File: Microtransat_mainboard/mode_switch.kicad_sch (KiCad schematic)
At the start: 3 parts

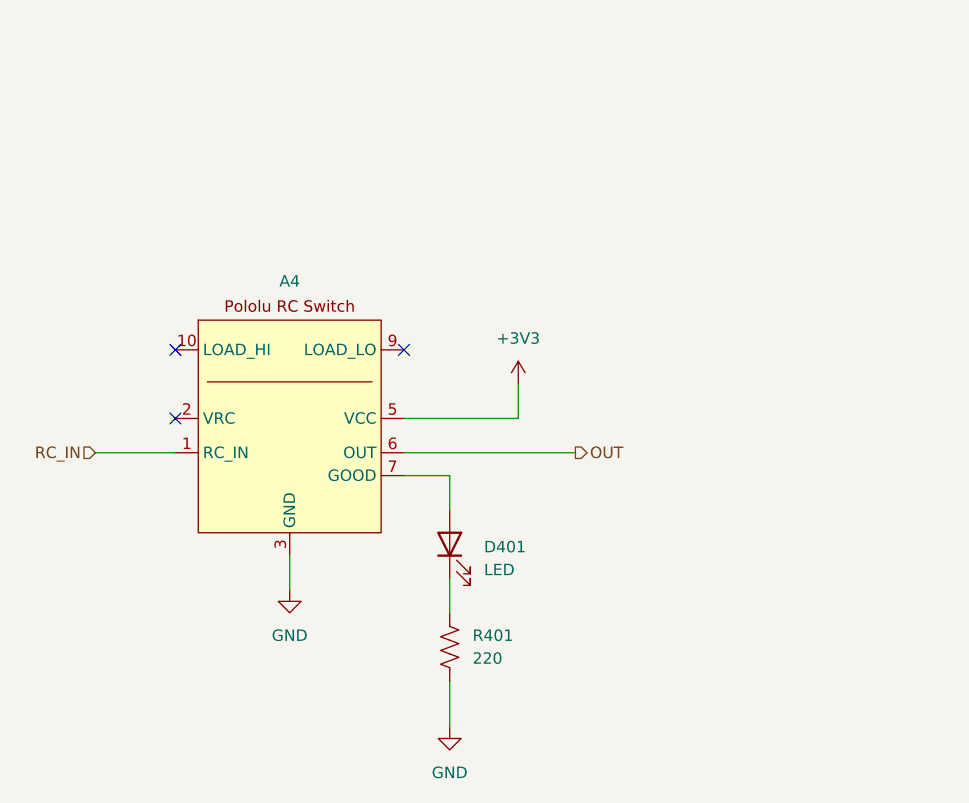
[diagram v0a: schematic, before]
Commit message: Added second RC switch for mode pin, added additional relay output, changed IMU to I2C
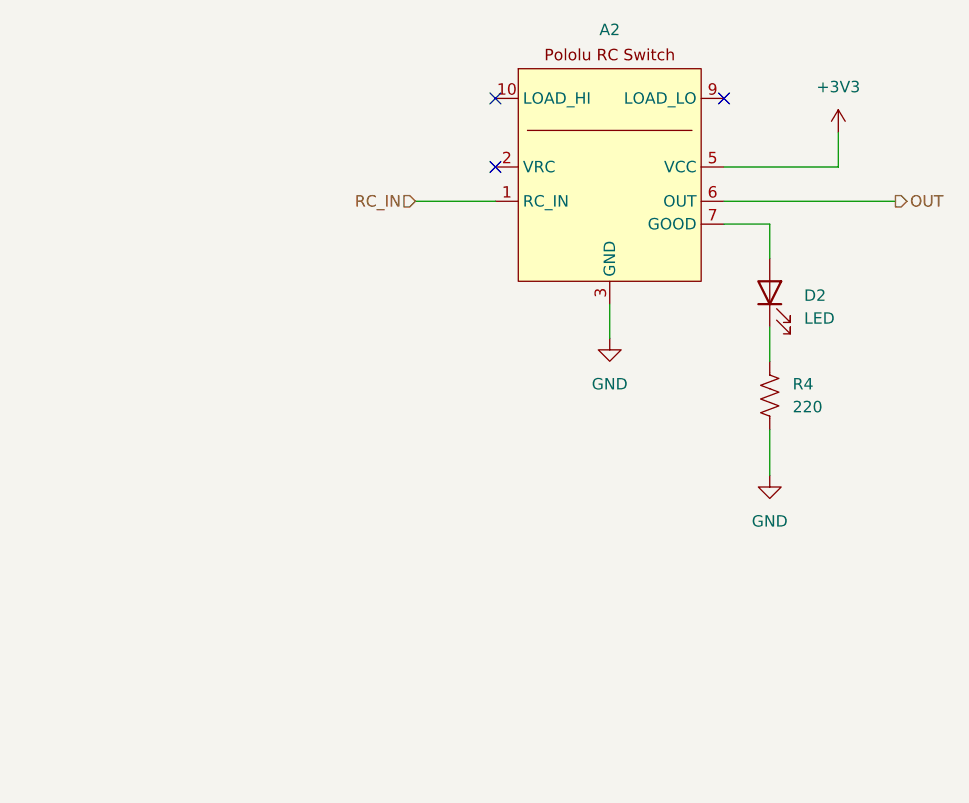
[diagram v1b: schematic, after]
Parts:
- removed A4: ~, Microtransat:Pololu RC Switch, symbol Microtransat:RC_Switch
- removed D401: LED, LED_SMD:LED_1206_3216Metric_Pad1.42x1.75mm_HandSolder, symbol Device:LED
- removed R401: 220, Resistor_SMD:R_1206_3216Metric_Pad1.30x1.75mm_HandSolder, symbol Device:R_US
- added A2: ~, Microtransat:Pololu RC Switch, symbol Microtransat:RC_Switch
- added D2: LED, LED_SMD:LED_1206_3216Metric_Pad1.42x1.75mm_HandSolder, symbol Device:LED
- added R4: 220, Resistor_SMD:R_1206_3216Metric_Pad1.30x1.75mm_HandSolder, symbol Device:R_US
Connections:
- net +3V3: now also A2.5 (VCC)
- net GND: now also A2.3 (GND), A2.4 (GND), A2.8 (GND), R4.2
- net LOAD_HI: now also A2.10 (LOAD_HI), A2.11 (LOAD_HI)
- net OUT: now also A2.6 (OUT)
- net RC_IN: now also A2.1 (RC_IN)
- new net: D2.1 (K), R4.1
- new net: A2.7 (GOOD), D2.2 (A)

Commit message: Finished silkscreen/outline changes
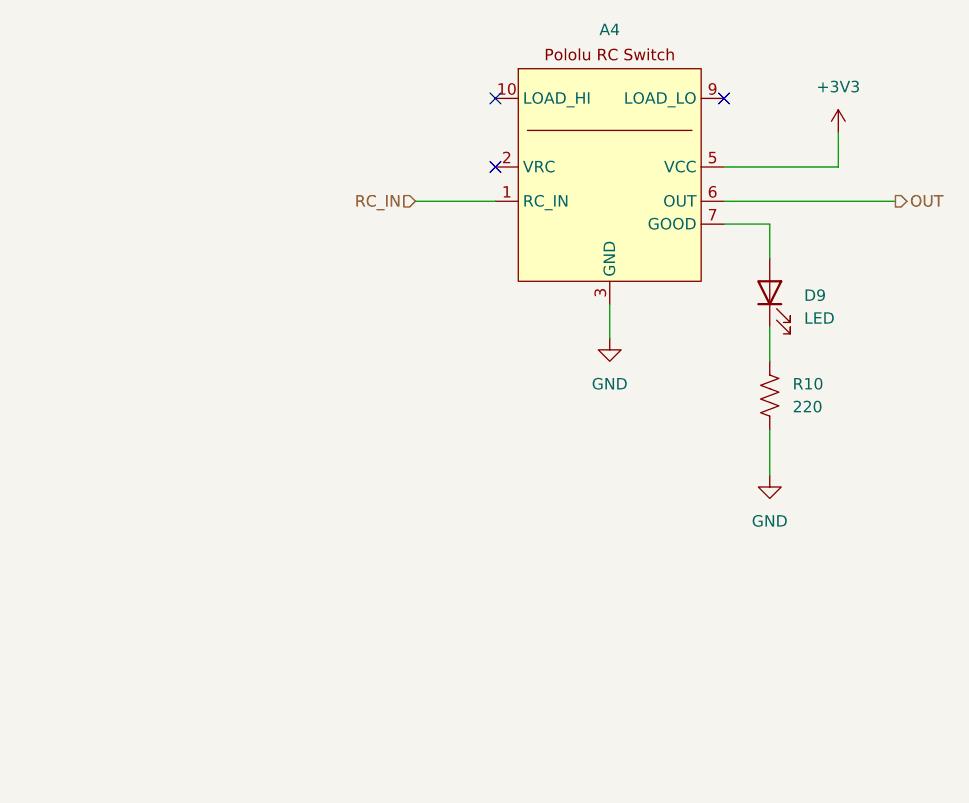
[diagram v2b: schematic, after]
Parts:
- renumbered A2 to A4, D2 to D9, R4 to R10
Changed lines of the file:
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@@
 		(dnp no)
 		(fields_autoplaced yes)
-		(property "Reference" "#PWR027"
+		(property "Reference" "#PWR049"
 			(at 139.7 88.9 0)
 			(effects
@@
 			(project "Microtransat_mainboard"
 				(path "/89914625-be83-416e-bb0d-b792f59b4aa6/59916782-1ad9-4ed5-b79a-f51cd480dbbd"
-					(reference "#PWR027")
+					(reference "#PWR049")
 					(unit 1)
 				)
@@
 		(dnp no)
 		(fields_autoplaced yes)
-		(property "Reference" "D2"
+		(property "Reference" "D9"
 			(at 161.29 77.7874 90)
 			(effects
@@
 			(project "Microtransat_mainboard"
 				(path "/89914625-be83-416e-bb0d-b792f59b4aa6/59916782-1ad9-4ed5-b79a-f51cd480dbbd"
-					(reference "D2")
+					(reference "D9")
 					(unit 1)
 				)
@@
 		(dnp no)
 		(fields_autoplaced yes)
-		(property "Reference" "#PWR030"
+		(property "Reference" "#PWR050"
 			(at 157.48 104.14 0)
 			(effects
@@
 			(project "Microtransat_mainboard"
 				(path "/89914625-be83-416e-bb0d-b792f59b4aa6/59916782-1ad9-4ed5-b79a-f51cd480dbbd"
-					(reference "#PWR030")
+					(reference "#PWR050")
 					(unit 1)
 				)
@@
 		(dnp no)
 		(fields_autoplaced yes)
-		(property "Reference" "A2"
+		(property "Reference" "A4"
 			(at 139.7 48.26 0)
 			(effects
@@
 			(project "Microtransat_mainboard"
 				(path "/89914625-be83-416e-bb0d-b792f59b4aa6/59916782-1ad9-4ed5-b79a-f51cd480dbbd"
-					(reference "A2")
+					(reference "A4")
 					(unit 1)
 				)
@@
 		(dnp no)
 		(fields_autoplaced yes)
-		(property "Reference" "R4"
+		(property "Reference" "R10"
 			(at 160.02 87.6299 0)
 			(effects
@@
 			(project "Microtransat_mainboard"
 				(path "/89914625-be83-416e-bb0d-b792f59b4aa6/59916782-1ad9-4ed5-b79a-f51cd480dbbd"
-					(reference "R4")
+					(reference "R10")
 					(unit 1)
 				)
@@
 		(dnp no)
 		(fields_autoplaced yes)
-		(property "Reference" "#PWR033"
+		(property "Reference" "#PWR051"
 			(at 165.1 63.5 0)
 			(effects
@@
 			(project "Microtransat_mainboard"
 				(path "/89914625-be83-416e-bb0d-b792f59b4aa6/59916782-1ad9-4ed5-b79a-f51cd480dbbd"
-					(reference "#PWR033")
-					(unit 1)
-				)
+					(reference "#PWR051")
+					(unit 1)
+				)

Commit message: Some small changes to silkscreen and component numbers
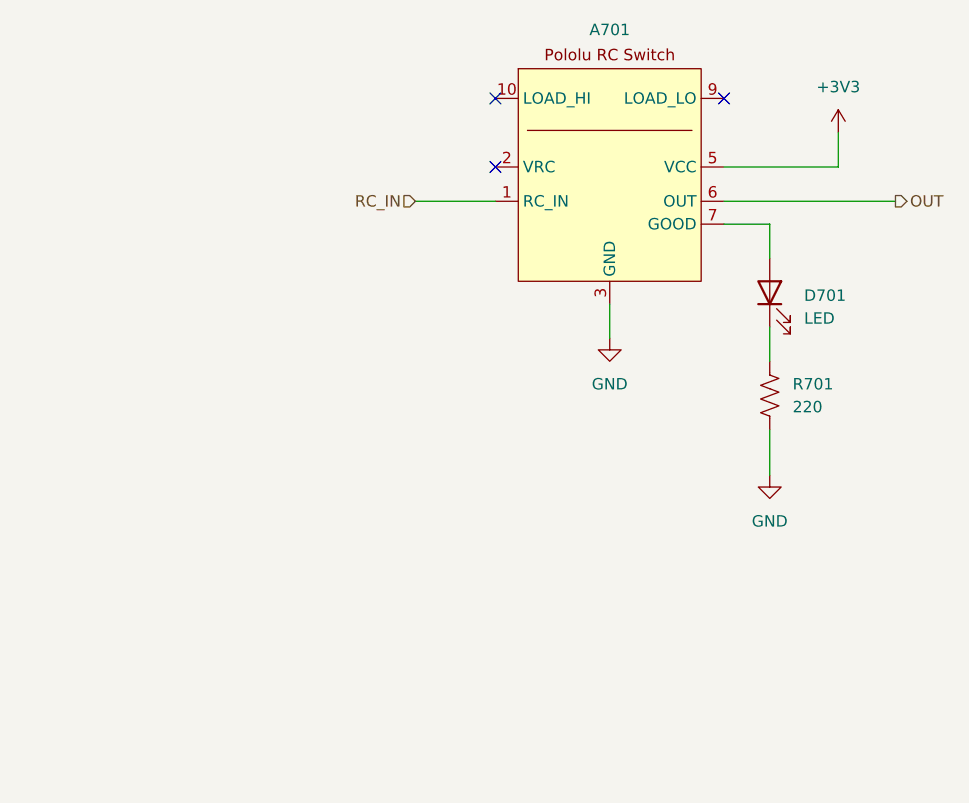
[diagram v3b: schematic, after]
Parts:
- renumbered A4 to A701, D9 to D701, R10 to R701
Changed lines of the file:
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@@
 		(dnp no)
 		(fields_autoplaced yes)
-		(property "Reference" "#PWR049"
+		(property "Reference" "#PWR0701"
 			(at 139.7 88.9 0)
 			(effects
@@
 			(project "Microtransat_mainboard"
 				(path "/89914625-be83-416e-bb0d-b792f59b4aa6/59916782-1ad9-4ed5-b79a-f51cd480dbbd"
-					(reference "#PWR049")
+					(reference "#PWR0701")
 					(unit 1)
 				)
@@
 		(dnp no)
 		(fields_autoplaced yes)
-		(property "Reference" "D9"
+		(property "Reference" "D701"
 			(at 161.29 77.7874 90)
 			(effects
@@
 			(project "Microtransat_mainboard"
 				(path "/89914625-be83-416e-bb0d-b792f59b4aa6/59916782-1ad9-4ed5-b79a-f51cd480dbbd"
-					(reference "D9")
+					(reference "D701")
 					(unit 1)
 				)
@@
 		(dnp no)
 		(fields_autoplaced yes)
-		(property "Reference" "#PWR050"
+		(property "Reference" "#PWR0702"
 			(at 157.48 104.14 0)
 			(effects
@@
 			(project "Microtransat_mainboard"
 				(path "/89914625-be83-416e-bb0d-b792f59b4aa6/59916782-1ad9-4ed5-b79a-f51cd480dbbd"
-					(reference "#PWR050")
+					(reference "#PWR0702")
 					(unit 1)
 				)
@@
 		(dnp no)
 		(fields_autoplaced yes)
-		(property "Reference" "A4"
+		(property "Reference" "A701"
 			(at 139.7 48.26 0)
 			(effects
@@
 			(project "Microtransat_mainboard"
 				(path "/89914625-be83-416e-bb0d-b792f59b4aa6/59916782-1ad9-4ed5-b79a-f51cd480dbbd"
-					(reference "A4")
+					(reference "A701")
 					(unit 1)
 				)
@@
 		(dnp no)
 		(fields_autoplaced yes)
-		(property "Reference" "R10"
+		(property "Reference" "R701"
 			(at 160.02 87.6299 0)
 			(effects
@@
 			(project "Microtransat_mainboard"
 				(path "/89914625-be83-416e-bb0d-b792f59b4aa6/59916782-1ad9-4ed5-b79a-f51cd480dbbd"
-					(reference "R10")
+					(reference "R701")
 					(unit 1)
 				)
@@
 		(dnp no)
 		(fields_autoplaced yes)
-		(property "Reference" "#PWR051"
+		(property "Reference" "#PWR0703"
 			(at 165.1 63.5 0)
 			(effects
@@
 			(project "Microtransat_mainboard"
 				(path "/89914625-be83-416e-bb0d-b792f59b4aa6/59916782-1ad9-4ed5-b79a-f51cd480dbbd"
-					(reference "#PWR051")
-					(unit 1)
-				)
+					(reference "#PWR0703")
+					(unit 1)
+				)
